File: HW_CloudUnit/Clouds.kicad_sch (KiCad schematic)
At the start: 23 parts, among them J1 Conn_01x06, J2 Conn_01x07, J3 Conn_01x04, U1 STM32G030F6Px, U2 AS5600L-ASOM, U3 DRV8313PWPR

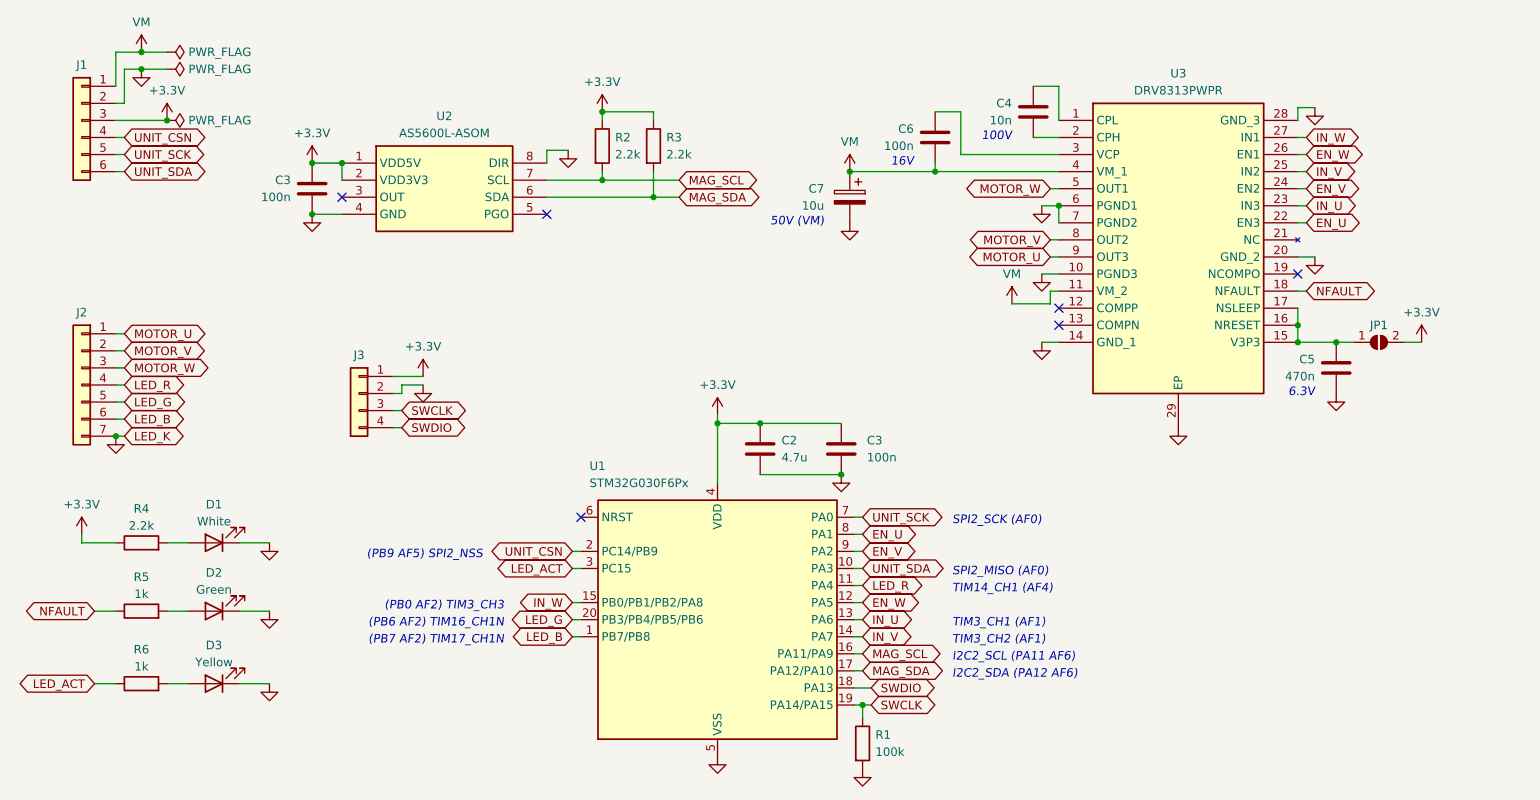
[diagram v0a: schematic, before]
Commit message: (WIP) Layout of driver board
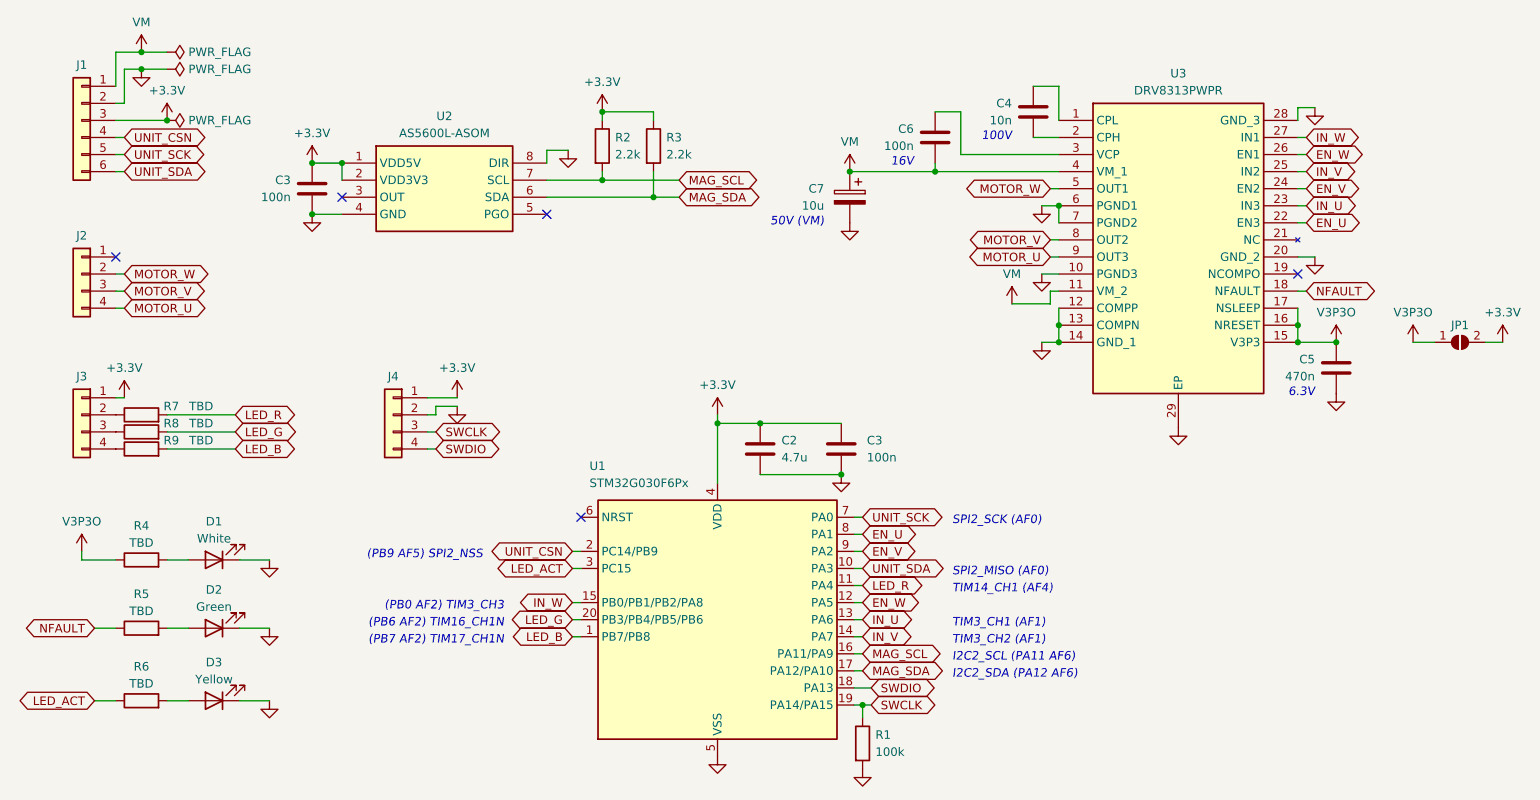
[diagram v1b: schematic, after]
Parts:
- removed J2: Conn_01x07, Connector_PinHeader_2.54mm:PinHeader_1x08_P2.54mm_Vertical, symbol Connector_Generic:Conn_01x07
- added J2: Conn_01x04, Connector_JST:JST_GH_SM04B-GHS-TB_1x04-1MP_P1.25mm_Horizontal, symbol Connector_Generic:Conn_01x04
- added J3: Conn_01x04, Connector_PinHeader_2.00mm:PinHeader_1x04_P2.00mm_Vertical, symbol Connector_Generic:Conn_01x04
- added R7, R8, R9: TBD, Resistor_SMD:R_0603_1608Metric, symbol Device:R
- D1, D2, D3: footprint LED_SMD:LED_0805_2012Metric -> LED_SMD:LED_0603_1608Metric
- J1: footprint Connector_PinHeader_2.54mm:PinHeader_1x10_P2.54mm_Vertical -> Connector_PinHeader_2.54mm:PinHeader_1x06_P2.54mm_Vertical
- J4: renamed from J3; footprint (none) -> Clouds_footprints:TestPoints_1x04_P2.0
- JP1: footprint (none) -> Jumper:SolderJumper-2_P1.3mm_Open_RoundedPad1.0x1.5mm
- R4: value 2.2k -> TBD
- R5, R6: value 1k -> TBD
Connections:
- net +3.3V: now also J3.1 (Pin_1); no longer R4.1
- net GND: now also U3.12 (COMPP), U3.13 (COMPN)
- net LED_B: now also R9.2
- net LED_G: now also R8.2
- net LED_R: now also R7.2
- net MOTOR_U: now also J2.4 (Pin_4)
- net MOTOR_V: now also J2.3 (Pin_3)
- net MOTOR_W: now also J2.2 (Pin_2)
- net V3P3O: now reaches C5.1, JP1.1 (A), U3.15 (V3P3), U3.16 (NRESET), U3.17 (NSLEEP)
- net V3P3O: now also R4.1
- new net: J3.4 (Pin_4), R9.1
- new net: J3.2 (Pin_2), R7.1
- new net: J3.3 (Pin_3), R8.1
- no-connect marks 6 -> 5
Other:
- moved on the sheet: D1, D2, D3, J4, JP1, R4, R5, R6

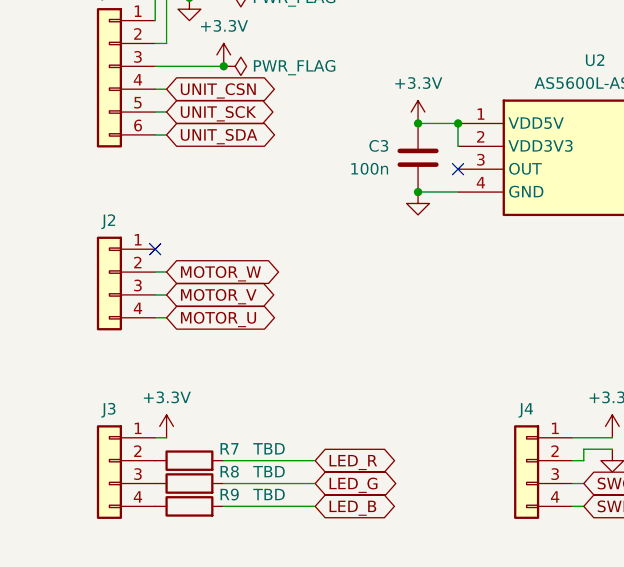
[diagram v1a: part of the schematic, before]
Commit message: Fix motor's wire order
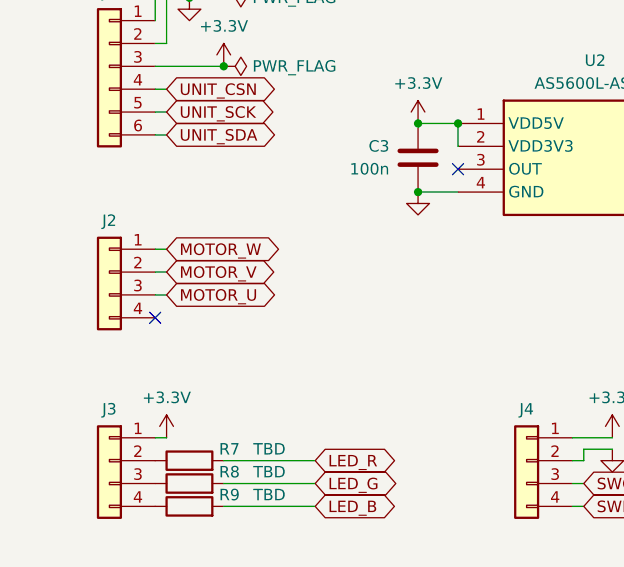
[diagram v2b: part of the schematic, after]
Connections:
- net MOTOR_U: now also J2.3 (Pin_3); no longer J2.4 (Pin_4)
- net MOTOR_V: now also J2.2 (Pin_2); no longer J2.3 (Pin_3)
- net MOTOR_W: now also J2.1 (Pin_1); no longer J2.2 (Pin_2)
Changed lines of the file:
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@@
   (no_connect (at 68.58 42.545))
   (no_connect (at 104.14 90.17))
-  (no_connect (at 34.925 51.435))
   (no_connect (at 210.82 53.975))
+  (no_connect (at 34.925 59.055))
   (wire (pts (xy 144.78 115.57) (xy 147.32 115.57))
     (stroke (width 0) (type default))
@@
     (stroke (width 0) (type default))
   )
+  (wire (pts (xy 34.925 51.435) (xy 36.195 51.435))
+    (stroke (width 0) (type default))
+  )
   (wire (pts (xy 130.81 83.82) (xy 142.875 83.82))
     (stroke (width 0) (type default))
@@
     (stroke (width 0) (type default))
   )
-  (wire (pts (xy 34.925 59.055) (xy 36.195 59.055))
-    (stroke (width 0) (type default))
-  )
   (wire (pts (xy 99.06 35.56) (xy 102.235 35.56))
     (stroke (width 0) (type default))
@@
     (stroke (width 0) (type default))
   )
+  (wire (pts (xy 81.28 72.39) (xy 85.725 72.39))
+    (stroke (width 0) (type default))
+  )
+  (wire (pts (xy 53.34 106.68) (xy 57.785 106.68))
+    (stroke (width 0) (type default))
+  )
+  (wire (pts (xy 212.09 41.275) (xy 210.82 41.275))
+    (stroke (width 0) (type default))
+  )
+  (wire (pts (xy 82.55 74.93) (xy 81.28 74.93))
+    (stroke (width 0) (type default))
+  )
+  (wire (pts (xy 53.34 96.52) (xy 57.785 96.52))
+    (stroke (width 0) (type default))
+  )
+  (wire (pts (xy 175.26 31.115) (xy 175.26 26.035))
+    (stroke (width 0) (type default))
+  )
+  (wire (pts (xy 114.935 42.545) (xy 99.06 42.545))
+    (stroke (width 0) (type default))
+  )
+  (wire (pts (xy 227.965 64.135) (xy 231.14 64.135))
+    (stroke (width 0) (type default))
+  )
+  (wire (pts (xy 213.36 51.435) (xy 210.82 51.435))
+    (stroke (width 0) (type default))
+  )
+  (wire (pts (xy 82.55 77.47) (xy 81.28 77.47))
+    (stroke (width 0) (type default))
+  )
+  (wire (pts (xy 212.09 33.655) (xy 210.82 33.655))
+    (stroke (width 0) (type default))
+  )
+  (wire (pts (xy 114.935 29.845) (xy 107.315 29.845))
+    (stroke (width 0) (type default))
+  )
+  (wire (pts (xy 34.925 53.975) (xy 36.195 53.975))
+    (stroke (width 0) (type default))
+  )
+  (wire (pts (xy 124.46 76.2) (xy 124.46 85.09))
+    (stroke (width 0) (type default))
+  )
+  (wire (pts (xy 36.195 28.575) (xy 36.195 23.495))
+    (stroke (width 0) (type default))
+  )
+  (wire (pts (xy 173.99 58.42) (xy 168.275 58.42))
+    (stroke (width 0) (type default))
+  )
+  (wire (pts (xy 102.87 107.95) (xy 104.14 107.95))
+    (stroke (width 0) (type default))
+  )
+  (wire (pts (xy 146.05 102.87) (xy 144.78 102.87))
+    (stroke (width 0) (type default))
+  )
+  (wire (pts (xy 146.05 97.79) (xy 144.78 97.79))
+    (stroke (width 0) (type default))
+  )
+  (wire (pts (xy 160.655 36.195) (xy 175.26 36.195))
+    (stroke (width 0) (type default))
+  )
+  (wire (pts (xy 146.05 118.11) (xy 144.78 118.11))
+    (stroke (width 0) (type default))
+  )
+  (wire (pts (xy 212.09 46.355) (xy 210.82 46.355))
+    (stroke (width 0) (type default))
+  )
+  (wire (pts (xy 147.32 118.11) (xy 146.05 118.11))
+    (stroke (width 0) (type default))
+  )
+  (wire (pts (xy 212.09 43.815) (xy 210.82 43.815))
+    (stroke (width 0) (type default))
+  )
+  (wire (pts (xy 172.72 53.975) (xy 175.26 53.975))
+    (stroke (width 0) (type default))
+  )
+  (wire (pts (xy 64.135 45.085) (xy 68.58 45.085))
+    (stroke (width 0) (type default))
+  )
+  (wire (pts (xy 212.09 38.735) (xy 210.82 38.735))
+    (stroke (width 0) (type default))
+  )
+  (wire (pts (xy 172.72 43.815) (xy 175.26 43.815))
+    (stroke (width 0) (type default))
+  )
+  (wire (pts (xy 146.05 107.95) (xy 144.78 107.95))
+    (stroke (width 0) (type default))
+  )
+  (wire (pts (xy 29.845 95.25) (xy 29.845 96.52))
+    (stroke (width 0) (type default))
+  )
   (wire (pts (xy 34.925 56.515) (xy 36.195 56.515))
-    (stroke (width 0) (type default))
-  )
-  (wire (pts (xy 81.28 72.39) (xy 85.725 72.39))
-    (stroke (width 0) (type default))
-  )
-  (wire (pts (xy 53.34 106.68) (xy 57.785 106.68))
-    (stroke (width 0) (type default))
-  )
-  (wire (pts (xy 212.09 41.275) (xy 210.82 41.275))
-    (stroke (width 0) (type default))
-  )
-  (wire (pts (xy 82.55 74.93) (xy 81.28 74.93))
-    (stroke (width 0) (type default))
-  )
-  (wire (pts (xy 53.34 96.52) (xy 57.785 96.52))
-    (stroke (width 0) (type default))
-  )
-  (wire (pts (xy 175.26 31.115) (xy 175.26 26.035))
-    (stroke (width 0) (type default))
-  )
-  (wire (pts (xy 34.925 53.975) (xy 36.195 53.975))
-    (stroke (width 0) (type default))
-  )
-  (wire (pts (xy 114.935 42.545) (xy 99.06 42.545))
-    (stroke (width 0) (type default))
-  )
-  (wire (pts (xy 227.965 64.135) (xy 231.14 64.135))
-    (stroke (width 0) (type default))
-  )
-  (wire (pts (xy 213.36 51.435) (xy 210.82 51.435))
-    (stroke (width 0) (type default))
-  )
-  (wire (pts (xy 82.55 77.47) (xy 81.28 77.47))
-    (stroke (width 0) (type default))
-  )
-  (wire (pts (xy 212.09 33.655) (xy 210.82 33.655))
-    (stroke (width 0) (type default))
-  )
-  (wire (pts (xy 114.935 29.845) (xy 107.315 29.845))
-    (stroke (width 0) (type default))
-  )
-  (wire (pts (xy 124.46 76.2) (xy 124.46 85.09))
-    (stroke (width 0) (type default))
-  )
-  (wire (pts (xy 36.195 28.575) (xy 36.195 23.495))
-    (stroke (width 0) (type default))
-  )
-  (wire (pts (xy 173.99 58.42) (xy 168.275 58.42))
-    (stroke (width 0) (type default))
-  )
-  (wire (pts (xy 102.87 107.95) (xy 104.14 107.95))
-    (stroke (width 0) (type default))
-  )
-  (wire (pts (xy 146.05 102.87) (xy 144.78 102.87))
-    (stroke (width 0) (type default))
-  )
-  (wire (pts (xy 146.05 97.79) (xy 144.78 97.79))
-    (stroke (width 0) (type default))
-  )
-  (wire (pts (xy 160.655 36.195) (xy 175.26 36.195))
-    (stroke (width 0) (type default))
-  )
-  (wire (pts (xy 146.05 118.11) (xy 144.78 118.11))
-    (stroke (width 0) (type default))
-  )
-  (wire (pts (xy 212.09 46.355) (xy 210.82 46.355))
-    (stroke (width 0) (type default))
-  )
-  (wire (pts (xy 147.32 118.11) (xy 146.05 118.11))
-    (stroke (width 0) (type default))
-  )
-  (wire (pts (xy 212.09 43.815) (xy 210.82 43.815))
-    (stroke (width 0) (type default))
-  )
-  (wire (pts (xy 172.72 53.975) (xy 175.26 53.975))
-    (stroke (width 0) (type default))
-  )
-  (wire (pts (xy 64.135 45.085) (xy 68.58 45.085))
-    (stroke (width 0) (type default))
-  )
-  (wire (pts (xy 212.09 38.735) (xy 210.82 38.735))
-    (stroke (width 0) (type default))
-  )
-  (wire (pts (xy 172.72 43.815) (xy 175.26 43.815))
-    (stroke (width 0) (type default))
-  )
-  (wire (pts (xy 146.05 107.95) (xy 144.78 107.95))
-    (stroke (width 0) (type default))
-  )
-  (wire (pts (xy 29.845 95.25) (xy 29.845 96.52))
     (stroke (width 0) (type default))
   )
@@
     )
   )
+  (global_label "MOTOR_W" (shape bidirectional) (at 36.195 51.435 0) (fields_autoplaced)
+    (effects (font (size 1.27 1.27)) (justify left))
+    (property "Intersheetrefs" "${INTERSHEET_REFS}" (at 49.0605 51.435 0)
+      (effects (font (size 1.27 1.27)) (justify left) hide)
+    )
+  )
+  (global_label "MOTOR_U" (shape bidirectional) (at 36.195 56.515 0) (fields_autoplaced)
+    (effects (font (size 1.27 1.27)) (justify left))
+    (property "Intersheetrefs" "${INTERSHEET_REFS}" (at 48.9396 56.515 0)
+      (effects (font (size 1.27 1.27)) (justify left) hide)
+    )
+  )
   (global_label "EN_V" (shape bidirectional) (at 146.05 95.25 0) (fields_autoplaced)
     (effects (font (size 1.27 1.27)) (justify left))
@@
     )
   )
-  (global_label "MOTOR_W" (shape bidirectional) (at 36.195 53.975 0) (fields_autoplaced)
-    (effects (font (size 1.27 1.27)) (justify left))
-    (property "Intersheetrefs" "${INTERSHEET_REFS}" (at 49.0605 53.975 0)
-      (effects (font (size 1.27 1.27)) (justify left) hide)
-    )
-  )
   (global_label "EN_V" (shape bidirectional) (at 212.09 41.275 0) (fields_autoplaced)
     (effects (font (size 1.27 1.27)) (justify left))
@@
     )
   )
-  (global_label "MOTOR_U" (shape bidirectional) (at 36.195 59.055 0) (fields_autoplaced)
-    (effects (font (size 1.27 1.27)) (justify left))
-    (property "Intersheetrefs" "${INTERSHEET_REFS}" (at 48.9396 59.055 0)
-      (effects (font (size 1.27 1.27)) (justify left) hide)
-    )
-  )
   (global_label "LED_B" (shape bidirectional) (at 102.87 107.95 180) (fields_autoplaced)
     (effects (font (size 1.27 1.27)) (justify right))
@@
     )
   )
+  (global_label "MOTOR_V" (shape bidirectional) (at 36.195 53.975 0) (fields_autoplaced)
+    (effects (font (size 1.27 1.27)) (justify left))
+    (property "Intersheetrefs" "${INTERSHEET_REFS}" (at 48.6977 53.975 0)
+      (effects (font (size 1.27 1.27)) (justify left) hide)
+    )
+  )
   (global_label "MAG_SDA" (shape bidirectional) (at 118.745 42.545 0) (fields_autoplaced)
     (effects (font (size 1.27 1.27)) (justify left))
@@
     )
   )
-  (global_label "MOTOR_V" (shape bidirectional) (at 36.195 56.515 0) (fields_autoplaced)
-    (effects (font (size 1.27 1.27)) (justify left))
-    (property "Intersheetrefs" "${INTERSHEET_REFS}" (at 48.6977 56.515 0)
-      (effects (font (size 1.27 1.27)) (justify left) hide)
-    )
-  )

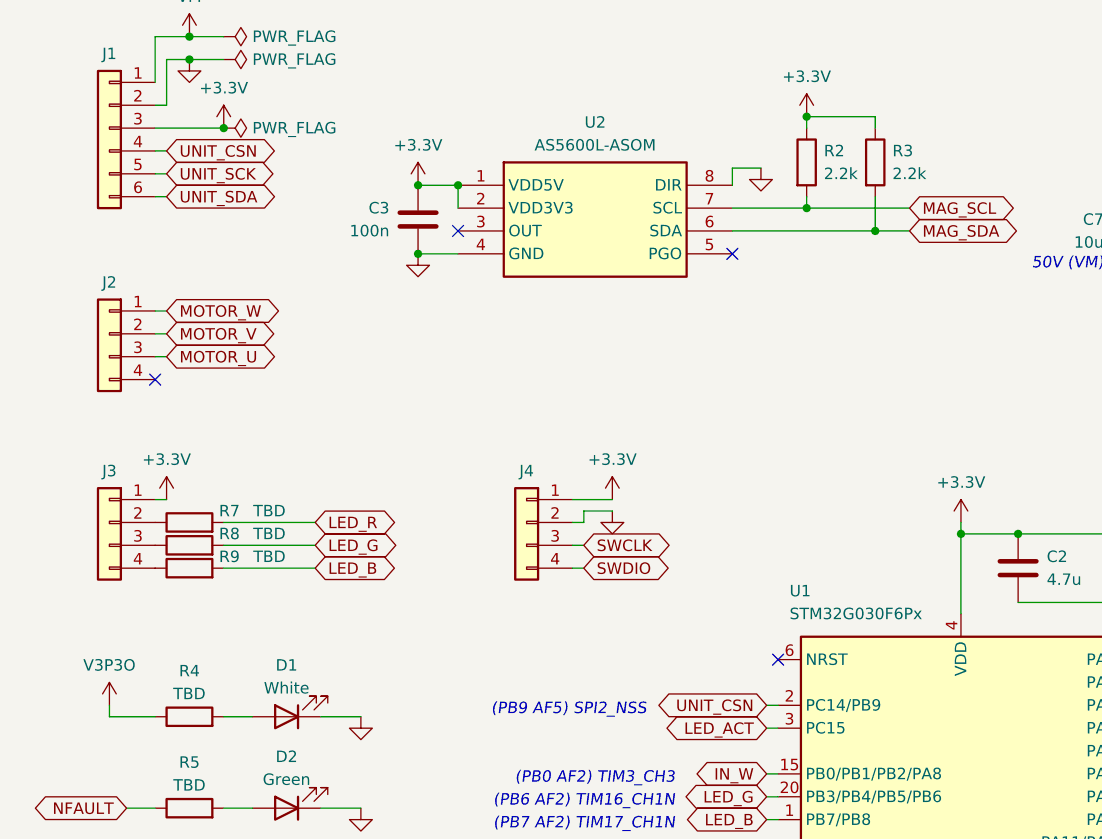
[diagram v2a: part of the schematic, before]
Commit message: Update boards with NPTH screw holes
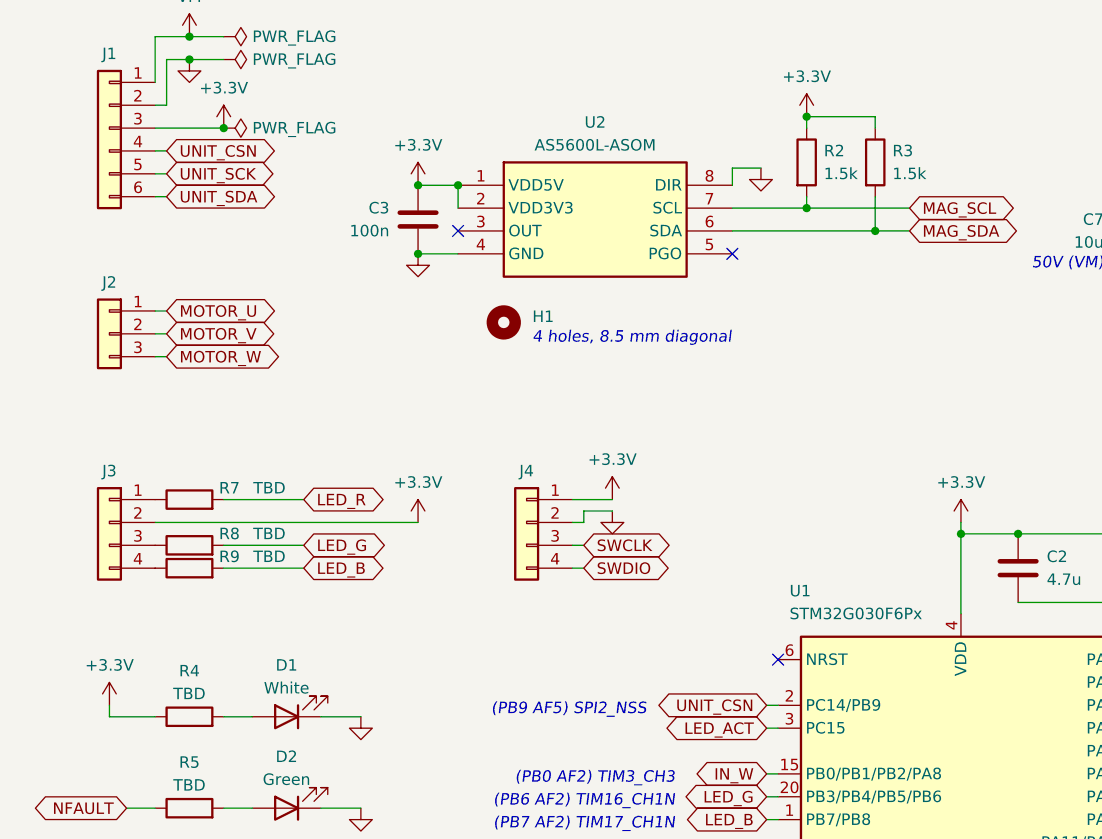
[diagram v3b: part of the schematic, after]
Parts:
- added H1: MountingHole, Clouds_footprints:MountingHoles_M1.4_Diag8.5, symbol Mechanical:MountingHole
- J2: value Conn_01x04 -> Conn_01x03; footprint Connector_JST:JST_GH_SM04B-GHS-TB_1x04-1MP_P1.25mm_Horizontal -> Connector_PinHeader_2.54mm:PinHeader_1x03_P2.54mm_Vertical; symbol Connector_Generic:Conn_01x04 -> Connector_Generic:Conn_01x03
- R2, R3: value 2.2k -> 1.5k
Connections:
- net +3.3V: now also J3.2 (Pin_2), R4.1; no longer J3.1 (Pin_1)
- net MOTOR_U: now also J2.1 (Pin_1); no longer J2.3 (Pin_3)
- net MOTOR_W: now also J2.3 (Pin_3); no longer J2.1 (Pin_1)
- net V3P3O: no longer R4.1
- net at R7.1: now also J3.1 (Pin_1); no longer J3.2 (Pin_2)
- no-connect marks 5 -> 4
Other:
- note added: "4 holes, 8.5 mm diagonal"
- moved on the sheet: R7
